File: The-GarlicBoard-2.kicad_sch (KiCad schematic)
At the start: 309 parts, among them J1 TYPE-C-31-M12_13, J2 Conn_01x04, J3 PAD_SQUARE_1MM, J4 PAD_SQUARE_1MM, J5 PAD_SQUARE_1MM, J6 PAD_SQUARE_1MM, SW1 ESC, SW10 S, SW11 X, SW12 L_CMD, SW13 E, SW14 D, SW15 C, SW16 R, SW17 F, SW18 V, SW19 FN_1, SW2 TAB, SW20 T, SW21 G, SW22 B, SW23 Y, SW24 H, SW25 N, SW26 SPACE, SW27 U, SW28 J, SW29 M, SW3 L_SHIFT, SW30 I, SW31 K, SW32 COMMA, SW33 R_CMD, SW34 O, SW35 L, SW36 PERIOD, SW37 P, SW38 SEMI_COLON, SW39 SLASH, SW4 L_CTRL, SW40 R_ALT, SW41 HYPHEN, SW42 APOSTROPHE, SW43 R_SHIFT, SW44 R_CTRL, SW45 EQUALS, SW46 RETURN, SW47 FN_2, SW48 BCK_SPC, SW49 7, SW5 Q, SW50 4, SW51 1, SW52 0, SW53 8, SW54 5, SW55 2, SW56 00, SW57 9, SW58 6, SW59 3, SW6 A, SW60 NUM_PER, SW61 MINUS, SW62 PLUS, SW63 ENTER, SW64 PAD_LOCK, SW65 RotaryEncoder_Switch, SW66 SW_Push, SW67 SW_Push, SW7 Z, SW8 L_ALT, SW9 W, U1 RP2040, U2 W25Q128JVS, U3 TPD4E05U06DQAR, U4 NCP1117-3.3_SOT223, U5 SN74LV1T34DCKR, Y1 12MHz

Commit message: Revision update
Removed USB connector and related components in favor of using Unified Daughterboard C3. Added 3D models to the footprints. Added JST connector for connecting to UD C3.
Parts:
- removed D66: SMF9.0CA, acheron_Components:D_SOD-123_Bidirectional, symbol Device:D_TVS
- removed F1: ASMD1206-150, Fuse:Fuse_1206_3216Metric, symbol Device:Polyfuse
- removed H6: MH_P, MountingHole:MountingHole_2.2mm_M2_DIN965_Pad, symbol Mechanical:MountingHole_Pad
- removed J1: TYPE-C-31-M12_13, Bonsai_C4:TYPE-C-31-M-12, symbol Unified-Daughterboard-rescue:TYPE-C-31-M12_13-acheronSymbols
- removed L1: 60R@100MHz, Inductor_SMD:L_1206_3216Metric, symbol Unified-Daughterboard-rescue:L_Core_Ferrite-Device
- removed R1, R2: 5.1k, Capacitor_SMD:C_0402_1005Metric, symbol Device:R
- removed U3: TPD4E05U06DQAR, acheron_Components:USON-10_2.5x1.0mm_P0.5mm, symbol Unified-Daughterboard-rescue:TPD4E05U06DQAR-acheronSymbols
- added H6: MH, MountingHole:MountingHole_2.2mm_M2, symbol Mechanical:MountingHole
- added J1: SM04B-SRSS-TB(LF)(SN), random-keyboard-parts:JST-SR-4, symbol Connector_Generic:Conn_01x04
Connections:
- net +5V: now also J1.1 (Pin_1)
- net GND: now also J1.4 (Pin_4)
- net DA+ renamed DN
- net DN: now also J1.2 (Pin_2)
- net DA- renamed DP
- net DP: now also J1.3 (Pin_3)
- no-connect marks 7 -> 5
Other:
- note added: "CONNECTOR TO UNIFIED DAUGHTERBOARD VOLTAGE REGULATOR"
- note removed: "USB AND ESD"
- moved on the sheet: C65, C66, C67, C68, C69, C70, C71, C72, C73, C74, C75, C76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

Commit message: Increased copper to copper tolerance to .2mm
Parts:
- removed C1, C10, C11, C17, C2, C20, C21, C22, C23, C24, C25, C26, C27, C28, C29, C3, C30, C31, C32, C33, C34, C35, C36, C37, C38, C39, C4, C40, C41, C42, C43, C44, C45, C46, C47, C48, C49, C5, C50, C51, C52, C53, C54, C55, C56, C57, C58, C59, C6, C60, C61, C62, C63, C64, C7, C8, C9: 0.1uF, Capacitor_SMD:C_0402_1005Metric, symbol Device:C
- removed LED1, LED10, LED11, LED12, LED13, LED14, LED15, LED16, LED17, LED18, LED19, LED2, LED20, LED21, LED22, LED23, LED24, LED25, LED26, LED27, LED28, LED29, LED3, LED30, LED31, LED32, LED33, LED34, LED35, LED36, LED37, LED38, LED39, LED4, LED40, LED41, LED42, LED43, LED44, LED45, LED46, LED47, LED48, LED49, LED5, LED50, LED51, LED52, LED53, LED54, LED55, LED56, LED57, LED58, LED59, LED6, LED60, LED61, LED62, LED63, LED64, LED7, LED8, LED9: YS-SK6812MINI-E, kbd:YS-SK6812MINI-E, symbol kbd:YS-SK6812MINI-E
- removed R13: 100k, Capacitor_SMD:C_0402_1005Metric, symbol Device:R
- removed U5: SN74LV1T34DCKR, Package_TO_SOT_SMD:SOT-353_SC-70-5, symbol Bonsai_C4:SN74LV1T34DCKR
- added C17: 22uF, Capacitor_Tantalum_SMD:CP_EIA-3216-10_Kemet-I, symbol Device:C_Polarized_Small_US
- added J6: PAD_SQUARE_1MM, Bonsai_C4:PAD_SQUARE_1MM, symbol Bonsai_C4:PAD_SQUARE_1MM
- added LED1, LED10, LED11, LED12, LED13, LED14, LED15, LED16, LED17, LED18, LED19, LED2, LED20, LED21, LED22, LED23, LED24, LED25, LED26, LED27, LED28, LED29, LED3, LED30, LED31, LED32, LED33, LED34, LED35, LED36, LED37, LED38, LED39, LED4, LED40, LED41, LED42, LED43, LED44, LED45, LED46, LED47, LED48, LED49, LED5, LED50, LED51, LED52, LED53, LED54, LED55, LED56, LED57, LED58, LED59, LED6, LED60, LED61, LED62, LED63, LED64, LED7, LED8, LED9: LED_ABGR, GarlicBoard v2:MHT151RGBCT-RGB-Reverse-Mount-1206-2, symbol Device:LED_ABGR
- added R6, R7: 2k, Resistor_SMD:R_0402_1005Metric, symbol Device:R
- added R8: 100k, Resistor_SMD:R_0402_1005Metric, symbol Device:R
- added R9: 20k, Resistor_SMD:R_0402_1005Metric, symbol Device:R
- added U2: IS31FL3733-QF, Package_DFN_QFN:QFN-48-1EP_6x6mm_P0.4mm_EP4.2x4.2mm, symbol Driver_LED:IS31FL3733-QF
- C12, C13, C15, C18: value 0.1uF -> 0.47uF
- D1, D10, D11, D12, D13, D14, D15, D16, D17, D18, D19, D2, D20, D21, D22, D23, D24, D25, D26, D27, D28, D29, D3, D30, D31, D32, D33, D34, D35, D36, D37, D38, D39, D4, D40, D41, D42, D43, D44, D45, D46, D47, D48, D49, D5, D50, D51, D52, D53, D54, D55, D56, D57, D58, D59, D6, D60, D61, D62, D63, D64, D65, D7, D8, D9: footprint Diode_SMD:D_0402_1005Metric -> Diode_SMD:D_SOD-323
- J1: value SM04B-SRSS-TB(LF)(SN) -> Molex Pico-EZMATE 781710004; footprint random-keyboard-parts:JST-SR-4 -> Connector_Molex:Molex_Pico-EZmate_78171-0004_1x04-1MP_P1.20mm_Vertical; LCSC Part No C160404 -> C588524; Manufacturer JST Sales America -> Molex; Manufacturer Part No SM04B-SRSS-TB(LF)(SN) -> 781710004
- R1: renamed from R3; footprint Capacitor_SMD:C_0402_1005Metric -> Resistor_SMD:R_0402_1005Metric
- R10, R11, R12: footprint Capacitor_SMD:C_0402_1005Metric -> Resistor_SMD:R_0402_1005Metric
- R2: renamed from R4; footprint Capacitor_SMD:C_0402_1005Metric -> Resistor_SMD:R_0402_1005Metric
- R3: renamed from R5; footprint Capacitor_SMD:C_0402_1005Metric -> Resistor_SMD:R_0402_1005Metric
- R4: renamed from R6; value DNF -> 2k; footprint Capacitor_SMD:C_0402_1005Metric -> Resistor_SMD:R_0402_1005Metric
- R5: renamed from R7; value DNF -> 2k; footprint Capacitor_SMD:C_0402_1005Metric -> Resistor_SMD:R_0402_1005Metric
- SW1, SW10, SW11, SW13, SW14, SW15, SW16, SW17, SW18, SW20, SW21, SW22, SW23, SW24, SW25, SW27, SW28, SW29, SW30, SW31, SW32, SW34, SW35, SW36, SW37, SW38, SW39, SW41, SW42, SW45, SW47, SW48, SW49, SW5, SW50, SW51, SW52, SW53, SW54, SW55, SW56, SW57, SW58, SW59, SW6, SW60, SW61, SW62, SW63, SW64, SW7, SW9: footprint MX_Hotswap:MX-Hotswap-1U -> GarlicBoard v2:MXOnly-1U-Hotswap
- SW12, SW2, SW33, SW4, SW40, SW44, SW8: footprint MX_Hotswap:MX-Hotswap-1.25U -> GarlicBoard v2:MXOnly-1.25U-Hotswap
- SW19, SW26: footprint MX_Hotswap:MX-Hotswap-2.75U -> GarlicBoard v2:MXOnly-2.75U-Hotswap
- SW3, SW46: footprint MX_Hotswap:MX-Hotswap-1.75U -> GarlicBoard v2:MXOnly-1.75U-Hotswap
- SW43: footprint MX_Hotswap:MX-Hotswap-2.25U -> GarlicBoard v2:MXOnly-2.25U-Hotswap
- SW65: footprint Keebio-Parts:RotaryEncoder_EC11 -> kbd_kicad_footprints-main:EVQWGD001
- renumbered C67 to C1, C76 to C10, C77 to C11, C68 to C2, C78 to C20, C79 to C21, C80 to C22, C65 to C23, C66 to C24, C69 to C3, C70 to C4, C71 to C5, C72 to C6, C73 to C7, C74 to C8, C75 to C9, H3 to H2, H5 to H3, H2 to H4, H4 to H5, J3 to J2, J4 to J3, J5 to J4, J6 to J5, J2 to J7, U2 to U3, U4 to U5
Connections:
- net +3V3: now also C12.2, R6.2, R7.2, U2.39 (VIO), U2.46 (~{SDB})
- net +5V: now also C17.1, U2.20 (PVCC), U2.29 (PVCC), U2.37 (AVCC), U2.38 (DVCC); no longer C12.1
- net COL0: now also U1.34 (GPIO22); no longer U1.27 (GPIO16)
- net COL1: now also U1.32 (GPIO21); no longer U1.28 (GPIO17)
- net COL2: now also U1.31 (GPIO20); no longer U1.29 (GPIO18)
- net COL4: now also U1.29 (GPIO18); no longer U1.31 (GPIO20)
- net COL5: now also U1.28 (GPIO17); no longer U1.32 (GPIO21)
- net COL6: now also U1.27 (GPIO16); no longer U1.34 (GPIO22)
- net COL7: now also U1.7 (GPIO5); no longer U1.6 (GPIO4)
- net COL8: now also U1.6 (GPIO4); no longer U1.7 (GPIO5)
- net GND: now also C12.1, C17.2, R8.2, R9.2, U2.12 (PGND), U2.34 (AGND), U2.43 (ADDR1), U2.44 (ADDR2), U2.48 (GND), U2.49 (GND), U2.5 (PGND); no longer C12.2
- net SCL: now also R7.1, U2.42 (SCL)
- net SDA: now also R6.1, U2.41 (SDA)
- net RGB: no longer names the net of U1.39 (GPIO27_ADC1)
- net RGB: now also J6.1
- new net: R9.1, U2.35 (RSET)
- new net: R8.1, U2.47 (IICRST)
- new net CS1: LED1.1 (A), LED17.1 (A), LED33.1 (A), LED49.1 (A), U2.16 (CS1)
- new net CS10: LED10.1 (A), LED26.1 (A), LED42.1 (A), LED58.1 (A), U2.26 (CS10)
- new net CS11: LED11.1 (A), LED27.1 (A), LED43.1 (A), LED59.1 (A), U2.27 (CS11)
- new net CS12: LED12.1 (A), LED28.1 (A), LED44.1 (A), LED60.1 (A), U2.28 (CS12)
- new net CS13: LED13.1 (A), LED29.1 (A), LED45.1 (A), LED61.1 (A), U2.30 (CS13)
- new net CS14: LED14.1 (A), LED30.1 (A), LED46.1 (A), LED62.1 (A), U2.31 (CS14)
- new net CS15: LED15.1 (A), LED31.1 (A), LED47.1 (A), LED63.1 (A), U2.32 (CS15)
- new net CS16: LED16.1 (A), LED32.1 (A), LED48.1 (A), LED64.1 (A), U2.33 (CS16)
- new net CS2: LED18.1 (A), LED2.1 (A), LED34.1 (A), LED50.1 (A), U2.17 (CS2)
- new net CS3: LED19.1 (A), LED3.1 (A), LED35.1 (A), LED51.1 (A), U2.18 (CS3)
- new net CS4: LED20.1 (A), LED36.1 (A), LED4.1 (A), LED52.1 (A), U2.19 (CS4)
- new net CS5: LED21.1 (A), LED37.1 (A), LED5.1 (A), LED53.1 (A), U2.21 (CS5)
- new net CS6: LED22.1 (A), LED38.1 (A), LED54.1 (A), LED6.1 (A), U2.22 (CS6)
- new net CS7: LED23.1 (A), LED39.1 (A), LED55.1 (A), LED7.1 (A), U2.23 (CS7)
- new net CS8: LED24.1 (A), LED40.1 (A), LED56.1 (A), LED8.1 (A), U2.24 (CS8)
- new net CS9: LED25.1 (A), LED41.1 (A), LED57.1 (A), LED9.1 (A), U2.25 (CS9)
- new net SW1: LED1.4 (RK), LED10.4 (RK), LED11.4 (RK), LED12.4 (RK), LED13.4 (RK), LED14.4 (RK), LED15.4 (RK), LED16.4 (RK), LED2.4 (RK), LED3.4 (RK), LED4.4 (RK), LED5.4 (RK), LED6.4 (RK), LED7.4 (RK), LED8.4 (RK), LED9.4 (RK), U2.2 (SW1)
- new net SW10: LED49.4 (RK), LED50.4 (RK), LED51.4 (RK), LED52.4 (RK), LED53.4 (RK), LED54.4 (RK), LED55.4 (RK), LED56.4 (RK), LED57.4 (RK), LED58.4 (RK), LED59.4 (RK), LED60.4 (RK), LED61.4 (RK), LED62.4 (RK), LED63.4 (RK), LED64.4 (RK), U2.13 (SW10)
- new net SW11: LED49.3 (GK), LED50.3 (GK), LED51.3 (GK), LED52.3 (GK), LED53.3 (GK), LED54.3 (GK), LED55.3 (GK), LED56.3 (GK), LED57.3 (GK), LED58.3 (GK), LED59.3 (GK), LED60.3 (GK), LED61.3 (GK), LED62.3 (GK), LED63.3 (GK), LED64.3 (GK), U2.14 (SW11)
- new net SW12: LED49.2 (BK), LED50.2 (BK), LED51.2 (BK), LED52.2 (BK), LED53.2 (BK), LED54.2 (BK), LED55.2 (BK), LED56.2 (BK), LED57.2 (BK), LED58.2 (BK), LED59.2 (BK), LED60.2 (BK), LED61.2 (BK), LED62.2 (BK), LED63.2 (BK), LED64.2 (BK), U2.15 (SW12)
- new net SW2: LED1.3 (GK), LED10.3 (GK), LED11.3 (GK), LED12.3 (GK), LED13.3 (GK), LED14.3 (GK), LED15.3 (GK), LED16.3 (GK), LED2.3 (GK), LED3.3 (GK), LED4.3 (GK), LED5.3 (GK), LED6.3 (GK), LED7.3 (GK), LED8.3 (GK), LED9.3 (GK), U2.3 (SW2)
- new net SW3: LED1.2 (BK), LED10.2 (BK), LED11.2 (BK), LED12.2 (BK), LED13.2 (BK), LED14.2 (BK), LED15.2 (BK), LED16.2 (BK), LED2.2 (BK), LED3.2 (BK), LED4.2 (BK), LED5.2 (BK), LED6.2 (BK), LED7.2 (BK), LED8.2 (BK), LED9.2 (BK), U2.4 (SW3)
- new net SW4: LED17.4 (RK), LED18.4 (RK), LED19.4 (RK), LED20.4 (RK), LED21.4 (RK), LED22.4 (RK), LED23.4 (RK), LED24.4 (RK), LED25.4 (RK), LED26.4 (RK), LED27.4 (RK), LED28.4 (RK), LED29.4 (RK), LED30.4 (RK), LED31.4 (RK), LED32.4 (RK), U2.6 (SW4)
- new net SW5: LED17.3 (GK), LED18.3 (GK), LED19.3 (GK), LED20.3 (GK), LED21.3 (GK), LED22.3 (GK), LED23.3 (GK), LED24.3 (GK), LED25.3 (GK), LED26.3 (GK), LED27.3 (GK), LED28.3 (GK), LED29.3 (GK), LED30.3 (GK), LED31.3 (GK), LED32.3 (GK), U2.7 (SW5)
- new net SW6: LED17.2 (BK), LED18.2 (BK), LED19.2 (BK), LED20.2 (BK), LED21.2 (BK), LED22.2 (BK), LED23.2 (BK), LED24.2 (BK), LED25.2 (BK), LED26.2 (BK), LED27.2 (BK), LED28.2 (BK), LED29.2 (BK), LED30.2 (BK), LED31.2 (BK), LED32.2 (BK), U2.8 (SW6)
- new net SW7: LED33.4 (RK), LED34.4 (RK), LED35.4 (RK), LED36.4 (RK), LED37.4 (RK), LED38.4 (RK), LED39.4 (RK), LED40.4 (RK), LED41.4 (RK), LED42.4 (RK), LED43.4 (RK), LED44.4 (RK), LED45.4 (RK), LED46.4 (RK), LED47.4 (RK), LED48.4 (RK), U2.9 (SW7)
- new net SW8: LED33.3 (GK), LED34.3 (GK), LED35.3 (GK), LED36.3 (GK), LED37.3 (GK), LED38.3 (GK), LED39.3 (GK), LED40.3 (GK), LED41.3 (GK), LED42.3 (GK), LED43.3 (GK), LED44.3 (GK), LED45.3 (GK), LED46.3 (GK), LED47.3 (GK), LED48.3 (GK), U2.10 (SW8)
- new net SW9: LED33.2 (BK), LED34.2 (BK), LED35.2 (BK), LED36.2 (BK), LED37.2 (BK), LED38.2 (BK), LED39.2 (BK), LED40.2 (BK), LED41.2 (BK), LED42.2 (BK), LED43.2 (BK), LED44.2 (BK), LED45.2 (BK), LED46.2 (BK), LED47.2 (BK), LED48.2 (BK), U2.11 (SW9)
- no-connect marks 5 -> 6
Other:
- note removed: "5V to drive SK6812-mini-e"
- note removed: "MCU TO LED STRAND"
- note removed: "RGB STRAND"
- moved on the sheet: C1, C10, C11, C2, C20, C21, C22, C23, C24, C3, C4, C5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

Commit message: Final additions and tweaks
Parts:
- removed J1: Molex Pico-EZMATE 781710004, Connector_Molex:Molex_Pico-EZmate_78171-0004_1x04-1MP_P1.20mm_Vertical, symbol Connector_Generic:Conn_01x04
- added J1: Molex Pico-EZMATE 781710004, Connector_Molex:Molex_Pico-EZmate_78171-0004_1x04-1MP_P1.20mm_Vertical, symbol Connector_Generic_MountingPin:Conn_01x04_MountingPin
- C1, C10, C11, C2, C22, C4, C6, C7, C8, C9: value 100n -> 100nF; Basic or Extended (none) -> Basic; LCSC (none) -> C1525; Manufacturer (none) -> Samsung Electro-Mechanics; Manufacturer Part No (none) -> CL05B104KO5NNNC
- C12, C13, C15, C18: Basic or Extended (none) -> Basic; LCSC (none) -> C47339; Manufacturer (none) -> Samsung Electro-Mechanics; Manufacturer Part No (none) -> CL05A474KP5NNNC
- C14, C16, C19: Basic or Extended (none) -> Basic; LCSC (none) -> C1525; Manufacturer (none) -> Samsung Electro-Mechanics; Manufacturer Part No (none) -> CL05B104KO5NNNC
- C17: Basic or Extended (none) -> Basic; LCSC (none) -> C7171; Manufacturer (none) -> Kyocera AVX; Manufacturer Part No (none) -> TAJA106K016RNJ
- C20, C21: value 27p -> 27pF; Basic or Extended (none) -> Basic; LCSC (none) -> C1557; Manufacturer (none) -> FH (Guangdong Fenghua Advanced Tech); Manufacturer Part No (none) -> 0402CG270J500NT
- C23, C24: value 10u -> 10uF; Basic or Extended (none) -> Basic; LCSC (none) -> C15525; Manufacturer (none) -> Samsung Electro-Mechanics; Manufacturer Part No (none) -> CL05A106MQ5NUNC
- C3, C5: value 1u -> 1uF; Basic or Extended (none) -> Basic; LCSC (none) -> C52923; Manufacturer (none) -> Samsung Electro-Mechanics; Manufacturer Part No (none) -> CL05A105KA5NQNC
- D1, D10, D11, D12, D13, D14, D15, D16, D17, D18, D19, D2, D20, D21, D22, D23, D24, D25, D26, D27, D28, D29, D3, D30, D31, D32, D33, D34, D35, D36, D37, D38, D39, D4, D40, D41, D42, D43, D44, D45, D46, D47, D48, D49, D5, D50, D51, D52, D53, D54, D55, D56, D57, D58, D59, D6, D60, D61, D62, D63, D64, D65, D7, D8, D9: Basic or Extended (none) -> Basic; LCSC (none) -> C191023; Manufacturer (none) -> Guangdong Hottech; Manufacturer Part No (none) -> 1N5819WS
- LED1, LED10, LED11, LED12, LED13, LED14, LED15, LED16, LED17, LED18, LED19, LED2, LED20, LED21, LED22, LED23, LED24, LED25, LED26, LED27, LED28, LED29, LED3, LED30, LED31, LED32, LED33, LED34, LED35, LED36, LED37, LED38, LED39, LED4, LED40, LED41, LED42, LED43, LED44, LED45, LED46, LED47, LED48, LED49, LED5, LED50, LED51, LED52, LED53, LED54, LED55, LED56, LED57, LED58, LED59, LED6, LED60, LED61, LED62, LED63, LED64, LED7, LED8, LED9: Basic or Extended (none) -> Extended; LCSC (none) -> C409782; Manufacturer (none) -> MEIHUA; Manufacturer Part No (none) -> MHT151RGBCT
- R1, R2: Basic or Extended (none) -> Extended; LCSC (none) -> C31439; Manufacturer (none) -> UNI-ROYAL(Uniroyal Elec); Manufacturer Part No (none) -> 0402WGF274JTCE
- R10, R11, R3: Basic or Extended (none) -> Basic; LCSC (none) -> C11702; Manufacturer (none) -> UNI-ROYAL(Uniroyal Elec); Manufacturer Part No (none) -> 0402WGF1001TCE
- R4, R5, R6, R7: Basic or Extended (none) -> Basic; LCSC (none) -> C4109; Manufacturer (none) -> UNI-ROYAL(Uniroyal Elec); Manufacturer Part No (none) -> 0402WGF2001TCE
- R8: Basic or Extended (none) -> Basic; LCSC (none) -> C25741; Manufacturer (none) -> UNI-ROYAL(Uniroyal Elec); Manufacturer Part No (none) -> 0402WGF1003TCE
- R9: Basic or Extended (none) -> Basic; LCSC (none) -> C25765; Manufacturer (none) -> UNI-ROYAL(Uniroyal Elec); Manufacturer Part No (none) -> 0402WGF2002TCE
- SW1, SW10, SW11, SW12, SW13, SW14, SW15, SW16, SW17, SW18, SW19, SW2, SW20, SW21, SW22, SW23, SW24, SW25, SW26, SW27, SW28, SW29, SW3, SW30, SW31, SW32, SW33, SW34, SW35, SW36, SW37, SW38, SW39, SW4, SW40, SW41, SW42, SW43, SW44, SW45, SW46, SW47, SW48, SW49, SW5, SW50, SW51, SW52, SW53, SW54, SW55, SW56, SW57, SW58, SW59, SW6, SW60, SW61, SW62, SW63, SW64, SW7, SW8, SW9: Basic or Extended (none) -> Extended; LCSC (none) -> C5184526; Manufacturer (none) -> Kailh/Kaihua; Manufacturer Part No (none) -> CPG151101S11-1
- SW66, SW67: Basic or Extended (none) -> Extended; LCSC (none) -> C231329; Manufacturer (none) -> Omron Electronics; Manufacturer Part No (none) -> B3U-1000P
- U1: Basic or Extended (none) -> Extended; LCSC (none) -> C2040; Manufacturer (none) -> Raspberry Pi; Manufacturer Part No (none) -> RP2040
- U2: Basic or Extended (none) -> Extended; LCSC (none) -> C2678773; Manufacturer (none) -> Lumissil Microsystems; Manufacturer Part No (none) -> IS31FL3733-QFLS4-TR
- U3: Basic or Extended (none) -> Basic; LCSC (none) -> C97521; Manufacturer (none) -> Winbond Elec; Manufacturer Part No (none) -> W25Q128JVSIQ
- U5: Basic or Extended (none) -> Extended; LCSC (none) -> C26537; Manufacturer (none) -> onsemi; Manufacturer Part No (none) -> NCP1117ST33T3G
- Y1: Basic or Extended (none) -> Basic; Manufacturer (none) -> Yangxing Tech; Manufacturer Part No (none) -> X322512MSB4SI
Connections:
- net +5V: now also J1.1 (Pin_1)
- net DN: now also J1.2 (Pin_2)
- net DP: now also J1.3 (Pin_3)
- net GND: now also J1.4 (Pin_4), J1.MP (MountPin)
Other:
- moved on the sheet: C20, C21, C22, C23, C24, H1, H2, H3, H4, H5, H6, J7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

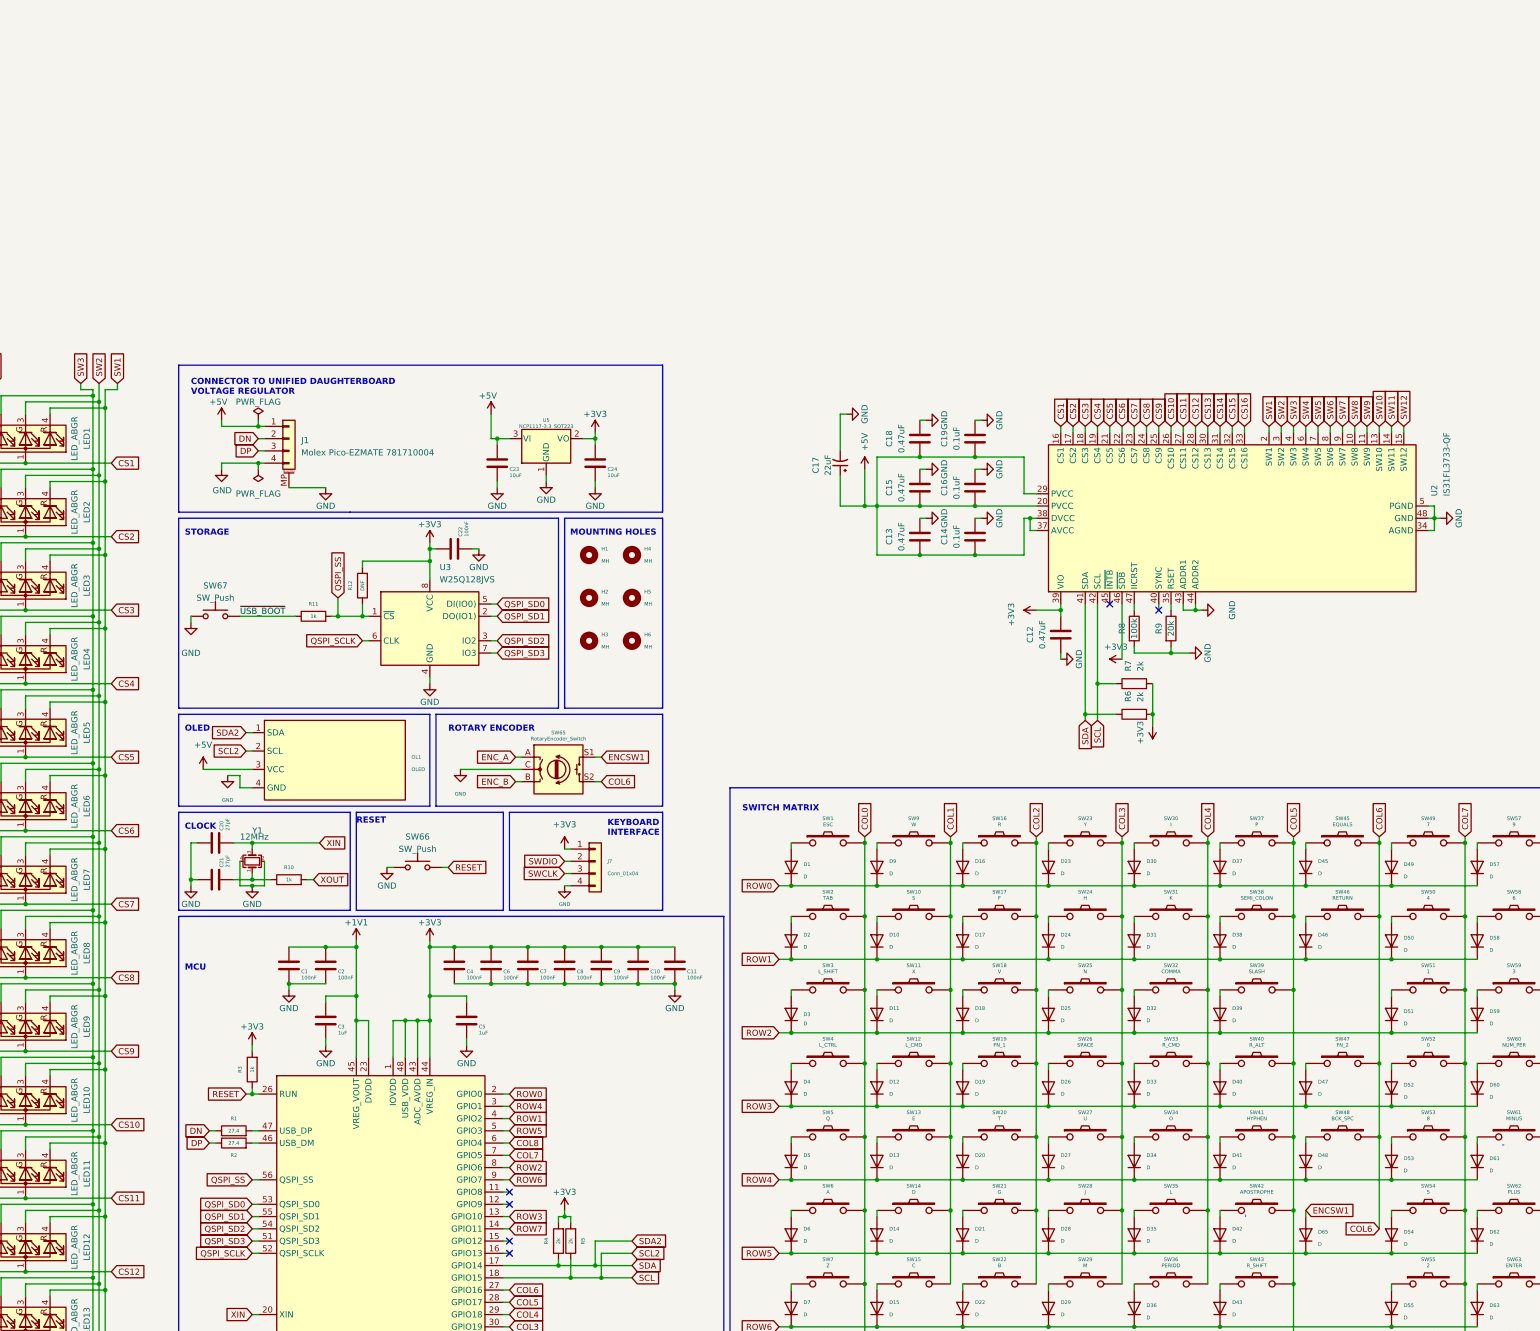
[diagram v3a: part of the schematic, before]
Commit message: Updated components
Added reverse polarity protection and debug LED
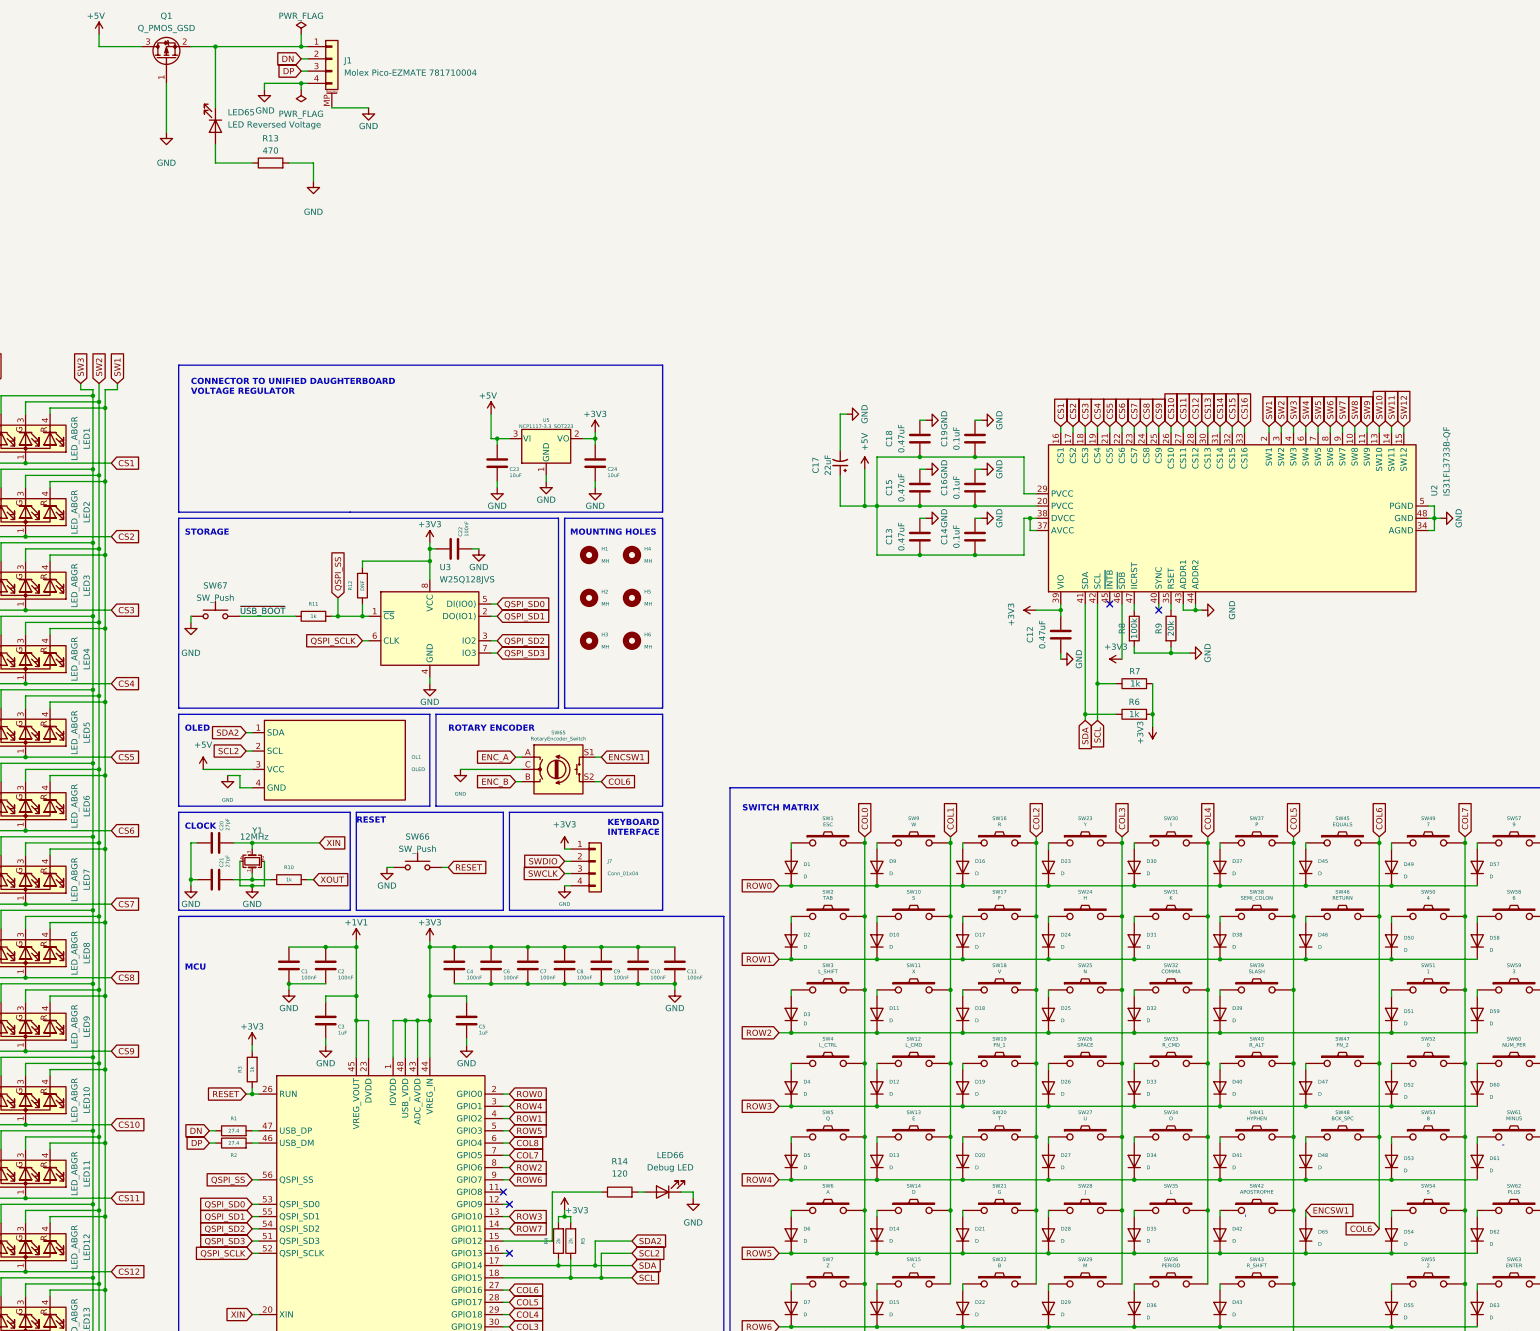
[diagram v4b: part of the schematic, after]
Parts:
- added LED65: LED Reversed Voltage, LED_SMD:LED_0603_1608Metric, symbol Device:LED
- added LED66: Debug LED, LED_SMD:LED_0603_1608Metric, symbol Device:LED
- added Q1: Q_PMOS_GSD, Package_TO_SOT_SMD:SOT-323_SC-70, symbol Device:Q_PMOS_GSD
- added R13: 470, Resistor_SMD:R_0402_1005Metric, symbol Device:R
- added R14: 120, Resistor_SMD:R_0402_1005Metric, symbol Device:R
- R6, R7: value 2k -> 1k; LCSC C4109 -> C11702; Manufacturer Part No 0402WGF2001TCE -> 0402WGF1001TCE
- SW65: footprint kbd_kicad_footprints-main:EVQWGD001 -> Rotary_Encoder:RotaryEncoder_Alps_EC11E-Switch_Vertical_H20mm
- U2: value IS31FL3733-QF -> IS31FL3733B-QF; LCSC C2678773 -> C5362338; Manufacturer Part No IS31FL3733-QFLS4-TR -> IS31FL3733B-QFLS4-TR
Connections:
- net +5V: now also Q1.3 (D); no longer J1.1 (Pin_1)
- net GND: now also LED66.1 (K), Q1.1 (G), R13.2
- net at U1.15 (GPIO12): now also R14.1
- new net: J1.1 (Pin_1), LED65.1 (K), Q1.2 (S)
- new net: LED66.2 (A), R14.2
- new net: LED65.2 (A), R13.1
- no-connect marks 6 -> 5
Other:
- moved on the sheet: J1

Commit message: Final update
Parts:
- SW1, SW10, SW11, SW13, SW14, SW15, SW16, SW17, SW18, SW20, SW21, SW22, SW23, SW24, SW25, SW27, SW28, SW29, SW30, SW31, SW32, SW34, SW35, SW36, SW37, SW38, SW39, SW41, SW42, SW45, SW47, SW48, SW49, SW5, SW50, SW51, SW53, SW54, SW55, SW57, SW58, SW59, SW6, SW60, SW61, SW62, SW63, SW64, SW7, SW9: footprint GarlicBoard v2:MXOnly-1U-Hotswap -> marbastlib-mx:SW_MX_HS_1u
- SW12, SW2, SW33, SW4, SW40, SW44, SW8: footprint GarlicBoard v2:MXOnly-1.25U-Hotswap -> marbastlib-mx:SW_MX_HS_1.25u
- SW19, SW26: footprint GarlicBoard v2:MXOnly-2.75U-Hotswap -> marbastlib-mx:SW_MX_HS_1u
- SW3, SW46: footprint GarlicBoard v2:MXOnly-1.75U-Hotswap -> marbastlib-mx:SW_MX_HS_1.75u
- SW43: footprint GarlicBoard v2:MXOnly-2.25U-Hotswap -> marbastlib-mx:SW_MX_HS_1u
- SW52: value 0 -> 00; footprint GarlicBoard v2:MXOnly-1U-Hotswap -> marbastlib-mx:SW_MX_HS_1u
- SW56: value 00 -> 0; footprint GarlicBoard v2:MXOnly-1U-Hotswap -> marbastlib-mx:SW_MX_HS_1u
